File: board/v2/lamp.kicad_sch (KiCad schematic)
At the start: 45 parts, among them J1 Conn_01x01_Female, J2 Conn_01x01_Female, J3 Conn_01x01_Female, J4 Conn_01x01_Female, J5 Conn_01x01_Female, J6 Conn_01x01_Female, J7 Conn_01x01_Female, U1 STM32L041F6Px, U2 TLV2333, U3 LP2985-33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

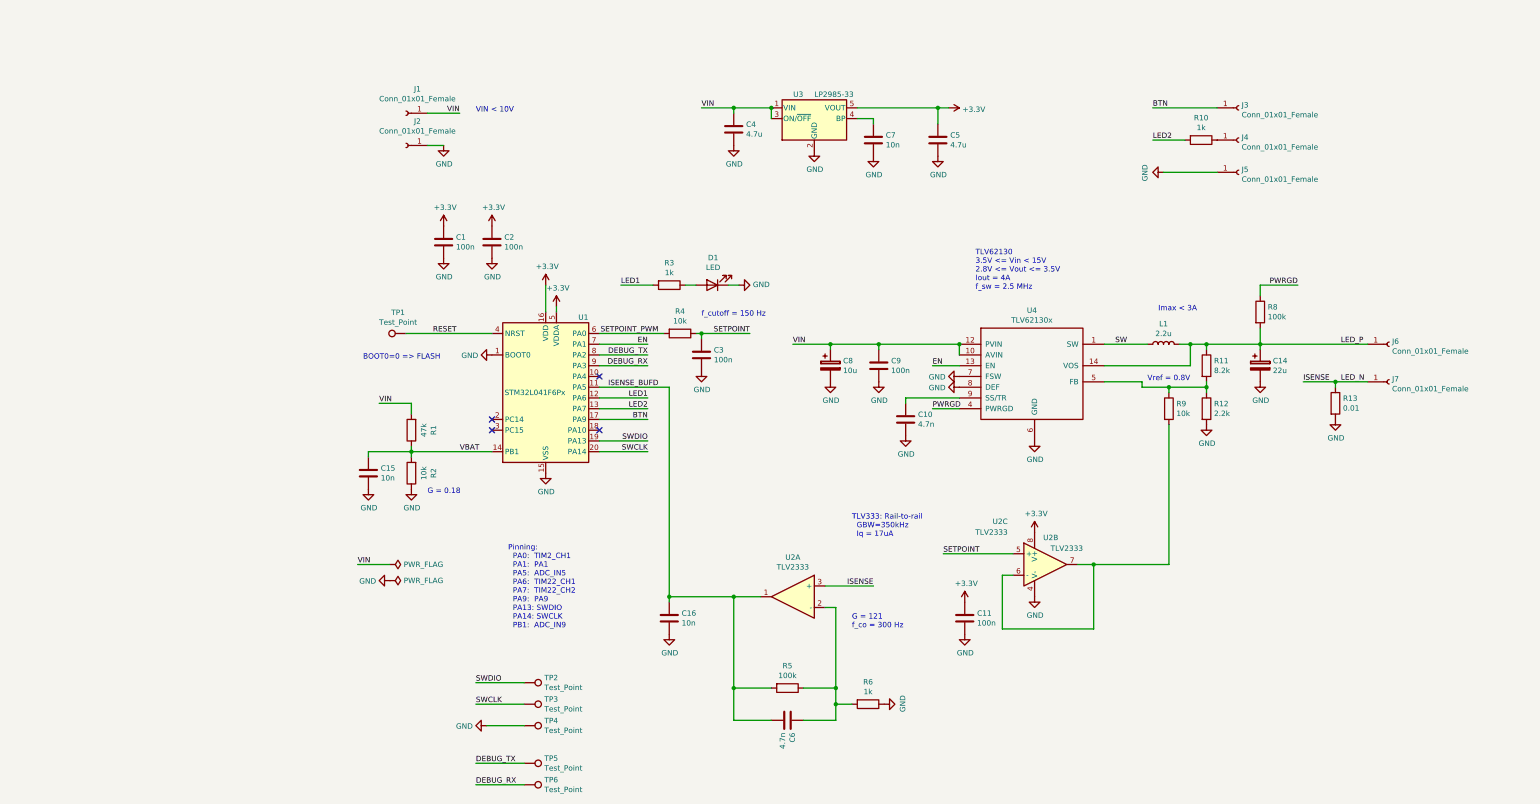
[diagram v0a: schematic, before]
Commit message: hardware: Revision 3
 * Increase board size to 28mm diameter
 * Use proper 1.27 mm pin socket for debug
 * Move to STM32L051K MCU
 * Drop thermal cut-out
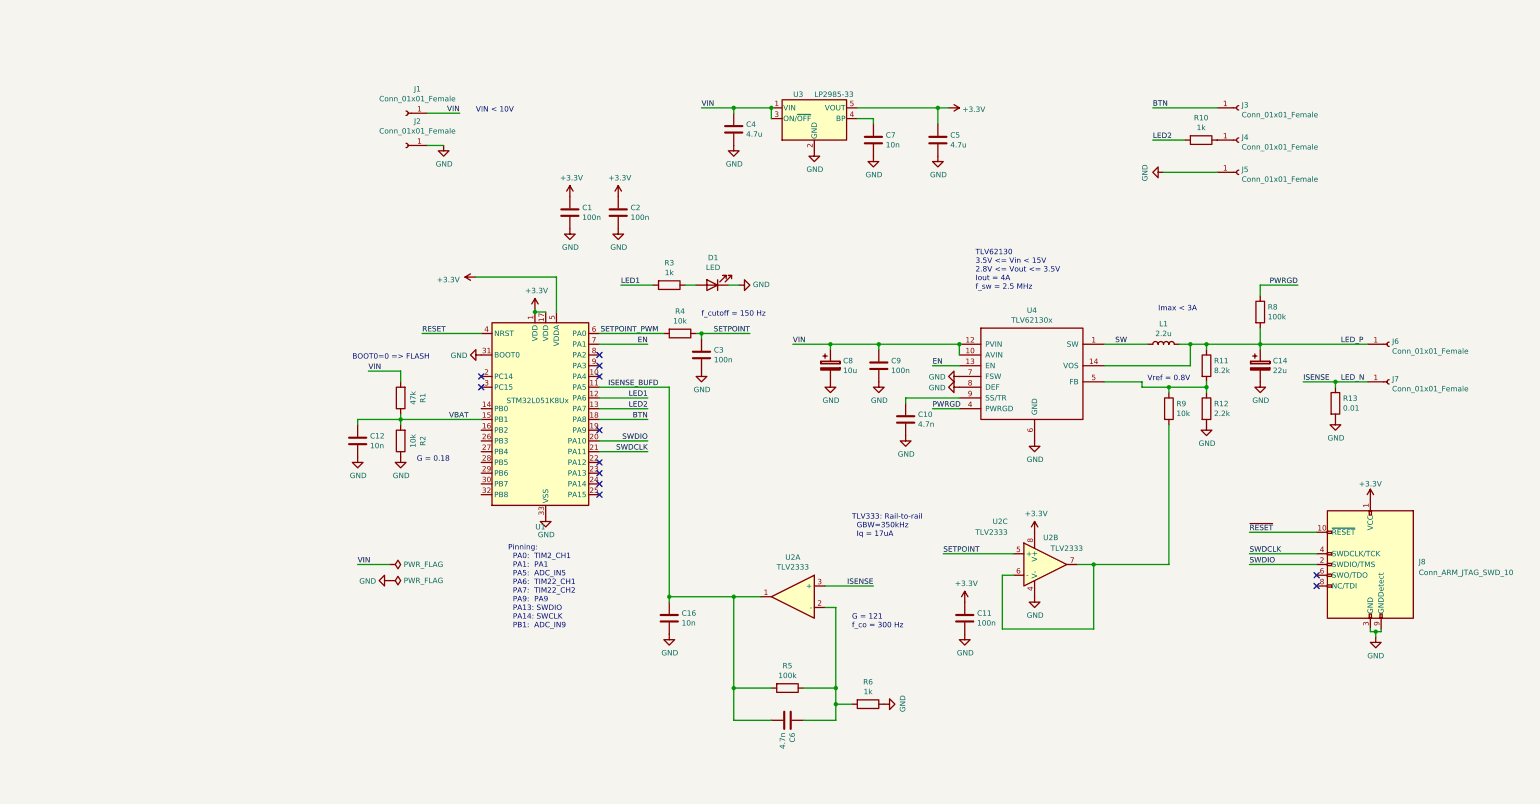
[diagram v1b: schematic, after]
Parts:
- removed C15: 10n, Capacitor_SMD:C_0603_1608Metric, symbol Device:C
- removed TP1, TP2, TP3, TP4, TP5, TP6: Test_Point, TestPoint:TestPoint_Pad_1.0x1.0mm, symbol Connector:Test_Point
- removed U1: STM32L041F6Px, Package_SO:TSSOP-20_4.4x6.5mm_P0.65mm, symbol MCU_ST_STM32L0:STM32L041F6Px
- added C12: 10n, Capacitor_SMD:C_0603_1608Metric, symbol Device:C
- added J8: Conn_ARM_JTAG_SWD_10, Connector_PinHeader_1.27mm:PinHeader_2x05_P1.27mm_Vertical_SMD, symbol Connector:Conn_ARM_JTAG_SWD_10
- added U1: STM32L051K8Ux, Package_DFN_QFN:QFN-32-1EP_5x5mm_P0.5mm_EP3.45x3.45mm, symbol MCU_ST_STM32L0:STM32L051K8Ux
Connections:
- net +3V3: now also J8.1 (VCC), U1.1 (VDD), U1.17 (VDD), U1.5 (VDDA)
- net BTN: now also U1.18 (PA8)
- net EN: now also U1.7 (PA1)
- net GND: now also C12.2, J8.3 (GND), J8.5 (GND), J8.9 (GNDDetect), U1.31 (BOOT0), U1.33 (VSS)
- net ISENSE_BUFD: now also U1.11 (PA5)
- net LED1: now also U1.12 (PA6)
- net LED2: now also U1.13 (PA7)
- net RESET: now also U1.4 (NRST)
- net SETPOINT_PWM: now also U1.6 (PA0)
- net SWDIO: now also J8.2 (SWDIO/TMS), U1.20 (PA10)
- net VBAT: now also C12.1, U1.15 (PB1)
- new net SWDCLK: J8.4 (SWDCLK/TCK), U1.21 (PA11)
- new net ~RESET: J8.10 (~RESET~)
- no-connect marks 4 -> 12
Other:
- moved on the sheet: C1, C2

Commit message: board: Move to STM32G071
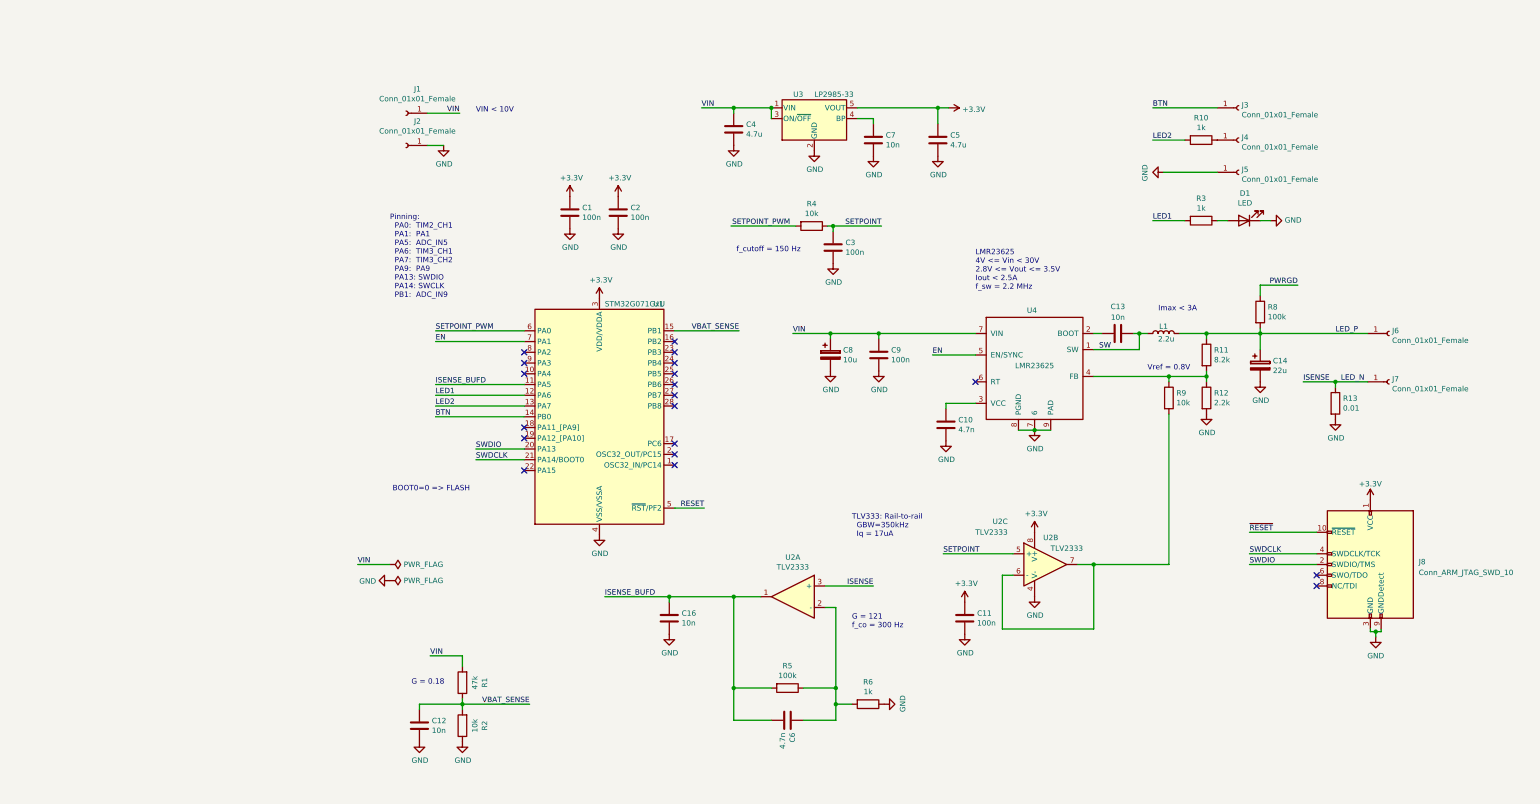
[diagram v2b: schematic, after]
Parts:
- removed U1: STM32L051K8Ux, Package_DFN_QFN:QFN-32-1EP_5x5mm_P0.5mm_EP3.45x3.45mm, symbol MCU_ST_STM32L0:STM32L051K8Ux
- added C13: 10n, Capacitor_SMD:C_0603_1608Metric, symbol Device:C
- added U1: STM32G071GxU, lamp:QFN-28_4.3x4.3_Pitch0.5mm, symbol lamp:STM32G071GxU
- U4: value TLV62130x -> LMR23625; footprint lamp:QFN-16_EP_3x3_Pitch0.5mm -> Package_SO:SOIC-8-1EP_3.9x4.9mm_P1.27mm_EP2.29x3mm_ThermalVias; symbol lamp:TLV62130x -> lamp:LMR23625
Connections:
- net +3V3: now also U1.3 (VDD/VDDA)
- net BTN: now also U1.14 (PB0)
- net EN: now also U4.5 (EN/SYNC), U1.7 (PA1); no longer U4.13 (EN)
- net GND: now also U4.9 (PAD), U1.4 (VSS/VSSA); no longer U4.15 (GND), U4.16 (GND), U4.17 (GND), U4.6 (GND)
- net ISENSE_BUFD: now also U1.11 (PA5)
- net LED1: now also U1.12 (PA6)
- net LED2: now also U1.13 (PA7)
- net LED_P: no longer U4.14 (VOS)
- net PWRGD: no longer U4.4 (PWRGD)
- net RESET: now also U1.5 (~RST~/PF2)
- net SETPOINT_PWM: now also U1.6 (PA0)
- net SW: now also C13.2; no longer U4.2 (SW), U4.3 (SW)
- net SWDCLK: now also U1.21 (PA14/BOOT0)
- net SWDIO: now also U1.20 (PA13)
- net VIN: now also U4.7 (VIN); no longer U4.10 (AVIN), U4.11 (PVIN), U4.12 (PVIN)
- net at C10.1: now also U4.3 (VCC); no longer U4.9 (SS/TR)
- net at R11.2, R12.1, R9.1: now also U4.4 (FB); no longer U4.5 (FB)
- net VBAT renamed VBAT_SENSE
- net VBAT_SENSE: now also U1.15 (PB1)
- new net: C13.1, U4.2 (BOOT)
- no-connect marks 12 -> 19
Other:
- note added: "LMR23625 4V <= Vin < 30V 2.8V <= Vout <= 3.5V Iout < 2.5A f_sw = 2.2 MHz"
- note added: "Pinning: PA0: TIM2_CH1 PA1: PA1 PA5: ADC_IN5 PA6: TIM3_CH1 PA7: TIM3_CH2 PA9: PA9 PA13: SWDIO PA14: SWCLK PB1: ADC_IN9"
- note removed: "Pinning: PA0: TIM2_CH1 PA1: PA1 PA5: ADC_IN5 PA6: TIM22_CH1 PA7: TIM22_CH2 PA9: PA9 PA13: SWDIO PA14: SWCLK PB1: ADC_IN9"
- note removed: "TLV62130 3.5V <= Vin < 15V 2.8V <= Vout <= 3.5V Iout = 4A f_sw = 2.5 MHz"
- moved on the sheet: C10, C12, C3, C8, C9, D1, J6, L1, R1, R11, R12, R2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

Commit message: hardware: Add reverse polarity protection
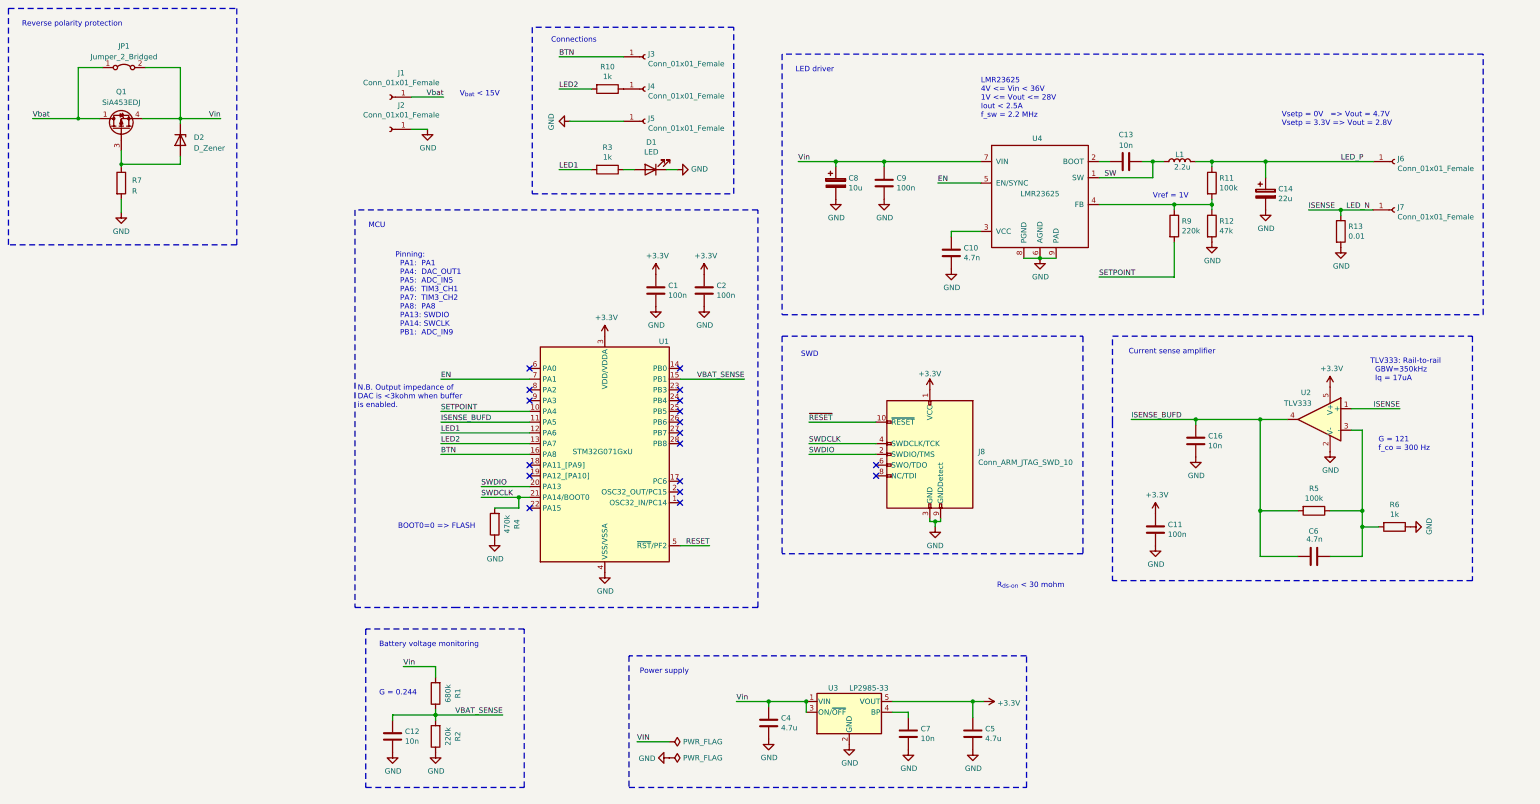
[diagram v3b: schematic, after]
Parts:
- removed C3: 100n, Capacitor_SMD:C_0603_1608Metric, symbol Device:C
- removed R8: 100k, Resistor_SMD:R_0603_1608Metric, symbol Device:R
- removed U2: TLV2333, Package_SO:TSSOP-8_3x3mm_P0.65mm, symbol Amplifier_Operational:OPA2333xxD
- added D2: D_Zener, Diode_SMD:D_SOD-323, symbol Device:D_Zener
- added JP1: Jumper_2_Bridged, Jumper:SolderJumper-2_P1.3mm_Bridged_Pad1.0x1.5mm, symbol Jumper:Jumper_2_Bridged
- added Q1: SiA453EDJ, Package_TO_SOT_SMD:Vishay_PowerPAK_SC70-6L_Single, symbol Transistor_FET:SiA453EDJ
- added R7: R, Resistor_SMD:R_0603_1608Metric, symbol Device:R
- added U2: TLV333, Package_TO_SOT_SMD:SOT-23-5, symbol Amplifier_Operational:LM321
- J8: MFG (none) -> CNC Tech; MPN (none) -> 3221-10-0300-00
- R1: value 47k -> 680k
- R11: value 8.2k -> 100k
- R12: value 2.2k -> 47k
- R2, R9: value 10k -> 220k
- R4: value 10k -> 470k
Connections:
- net +3V3: now also U2.5 (V+)
- net BTN: now also U1.16 (PA8); no longer U1.14 (PB0)
- net GND: now also R4.1, U4.6 (AGND), R7.2, U2.2 (V-); no longer U4.7 (VIN)
- net ISENSE: now also U2.1 (+)
- net ISENSE_BUFD: now also U2.4
- net SETPOINT: now also R9.2, U1.10 (PA4); no longer R4.1
- net SWDCLK: now also R4.2
- net VIN: no longer C4.1, C8.1, C9.1, J1.1 (Pin_1), R1.2, U3.1 (VIN), U3.3 (ON/~OFF~), U4.7 (VIN)
- net at C6.1, R5.1, R6.2: now also U2.3 (-)
- net SETPOINT_PWM: no longer names the net of U1.6 (PA0)
- net SETPOINT_PWM: no longer R4.2
- new net: D2.2 (A), Q1.3 (G), R7.1
- new net Vbat: J1.1 (Pin_1), JP1.1 (A), Q1.1 (D)
- new net Vin: C4.1, C8.1, C9.1, D2.1 (K), JP1.2 (B), Q1.4 (S), R1.2, U3.1 (VIN), U3.3 (ON/~OFF~), U4.7 (VIN)
- no-connect marks 19 -> 18
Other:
- note added: "Battery voltage monitoring"
- note added: "Connections"
- note added: "Current sense amplifier"
- note added: "G = 0.244"
- note added: "LED driver"
- note added: "LMR23625 4V <= Vin < 36V 1V <= Vout <= 28V Iout < 2.5A f_sw = 2.2 MHz"
- note added: "MCU"
- note added: "N.B. Output impedance of DAC is <3kohm when buffer is enabled."
- note added: "Pinning: PA1: PA1 PA4: DAC_OUT1 PA5: ADC_IN5 PA6: TIM3_CH1 PA7: TIM3_CH2 PA8: PA8 PA13: SWDIO PA14: SWCLK PB1: ADC_IN9"
- note added: "Power supply"
- note added: "R_{ds-on} < 30 mohm"
- note added: "Reverse polarity protection"
- note added: "SWD"
- note added: "V_{bat} < 15V"
- note added: "Vref = 1V"
- note added: "Vsetp = 0V => Vout = 4.7V Vsetp = 3.3V => Vout = 2.8V"
- note removed: "G = 0.18"
- note removed: "Imax < 3A"
- note removed: "LMR23625 4V <= Vin < 30V 2.8V <= Vout <= 3.5V Iout < 2.5A f_sw = 2.2 MHz"
- note removed: "Pinning: PA0: TIM2_CH1 PA1: PA1 PA5: ADC_IN5 PA6: TIM3_CH1 PA7: TIM3_CH2 PA9: PA9 PA13: SWDIO PA14: SWCLK PB1: ADC_IN9"
- note removed: "VIN < 10V"
- note removed: "Vref = 0.8V"
- note removed: "f_cutoff = 150 Hz"
- moved on the sheet: C1, C10, C11, C12, C13, C14, C16, C2, C4, C5, C6, C7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

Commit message: hardware: More fiddling
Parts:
- C14, C8: symbol Device:CP -> Device:C_Polarized
- D1: value LED -> GREEN
